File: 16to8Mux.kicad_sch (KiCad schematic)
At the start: 4 parts

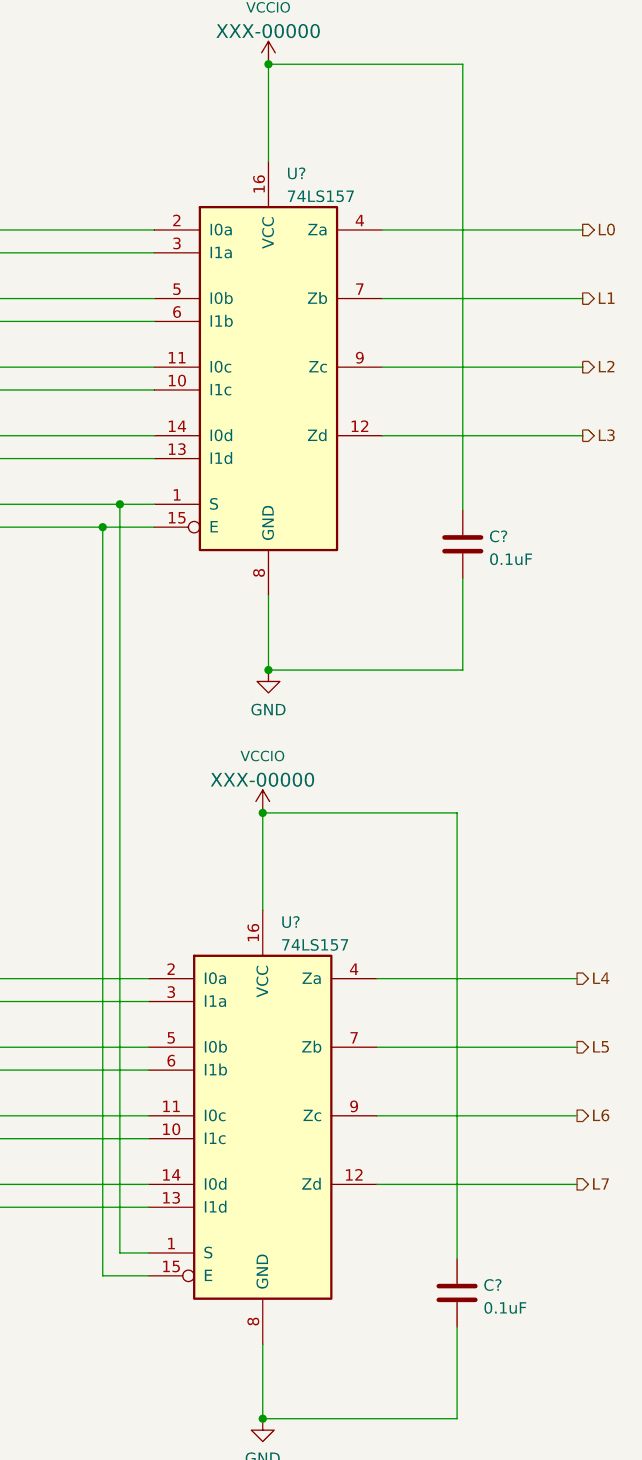
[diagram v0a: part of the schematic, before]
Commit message: Even more simplification and be able to reset feathers separately from the chipset
Makes it possible to also reset them if needed as well
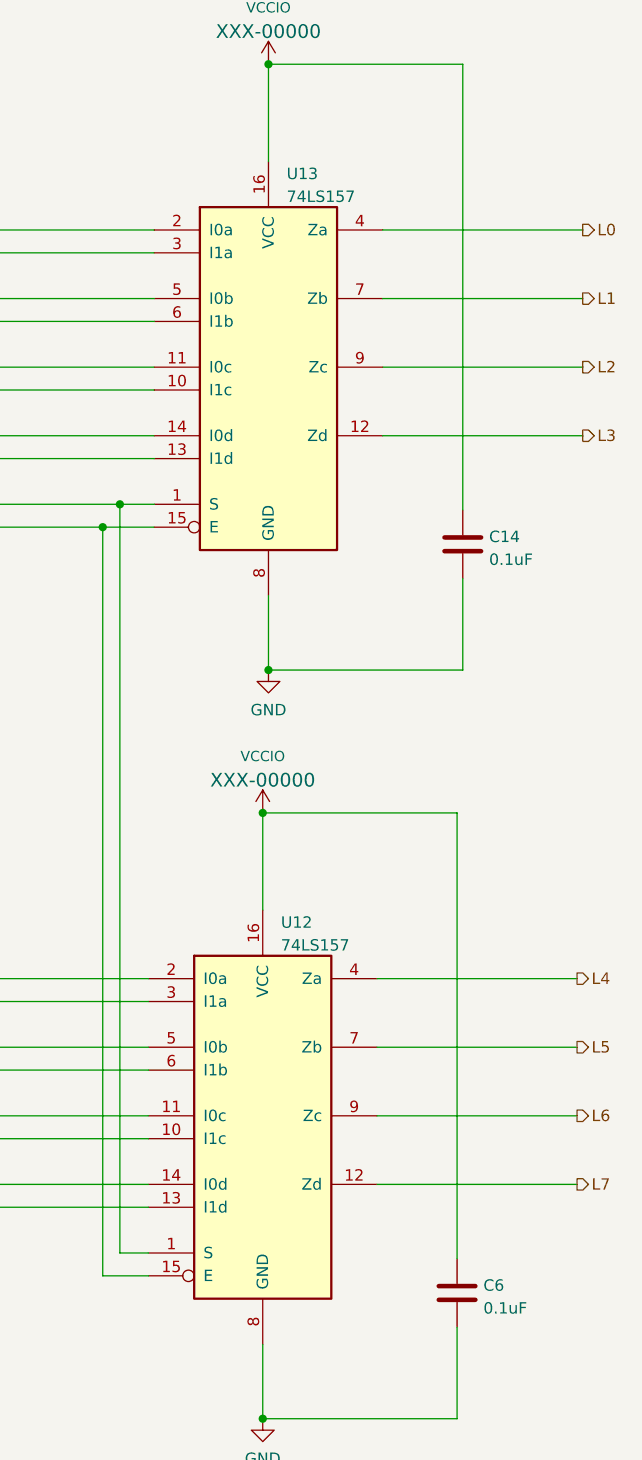
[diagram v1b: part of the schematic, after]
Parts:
- C14, C6: renamed from C?; footprint (none) -> Capacitor_SMD:C_0805_2012Metric_Pad1.18x1.45mm_HandSolder
- U12, U13: renamed from U?; footprint (none) -> Package_DIP:DIP-16_W7.62mm_Socket
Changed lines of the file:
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@@
   (symbol (lib_id "Device:C") (at 99.06 85.09 0) (unit 1)
     (in_bom yes) (on_board yes) (fields_autoplaced)
-    (property "Reference" "C?" (id 0) (at 101.981 84.2553 0)
+    (property "Reference" "C14" (id 0) (at 101.981 84.2553 0)
       (effects (font (size 1.27 1.27)) (justify left))
     )
@@
       (effects (font (size 1.27 1.27)) (justify left))
     )
-    (property "Footprint" "" (id 2) (at 100.0252 88.9 0)
+    (property "Footprint" "Capacitor_SMD:C_0805_2012Metric_Pad1.18x1.45mm_HandSolder" (id 2) (at 100.0252 88.9 0)
       (effects (font (size 1.27 1.27)) hide)
     )
@@
   (symbol (lib_id "power:GND") (at 76.835 182.245 0) (unit 1)
     (in_bom yes) (on_board yes) (fields_autoplaced)
-    (property "Reference" "#PWR?" (id 0) (at 76.835 188.595 0)
+    (property "Reference" "#PWR038" (id 0) (at 76.835 188.595 0)
       (effects (font (size 1.27 1.27)) hide)
     )
@@
   (symbol (lib_id "power:GND") (at 77.47 99.06 0) (unit 1)
     (in_bom yes) (on_board yes) (fields_autoplaced)
-    (property "Reference" "#PWR?" (id 0) (at 77.47 105.41 0)
+    (property "Reference" "#PWR039" (id 0) (at 77.47 105.41 0)
       (effects (font (size 1.27 1.27)) hide)
     )
@@
   (symbol (lib_id "SparkFun-PowerSymbols:VCCIO") (at 77.47 31.75 0) (unit 1)
     (in_bom yes) (on_board yes) (fields_autoplaced)
-    (property "Reference" "#SUPPLY?" (id 0) (at 78.74 31.75 0)
+    (property "Reference" "#SUPPLY07" (id 0) (at 78.74 31.75 0)
       (effects (font (size 1.143 1.143)) (justify left bottom) hide)
     )
@@
   (symbol (lib_id "Device:C") (at 98.425 168.275 0) (unit 1)
     (in_bom yes) (on_board yes) (fields_autoplaced)
-    (property "Reference" "C?" (id 0) (at 101.346 167.4403 0)
+    (property "Reference" "C6" (id 0) (at 101.346 167.4403 0)
       (effects (font (size 1.27 1.27)) (justify left))
     )
@@
       (effects (font (size 1.27 1.27)) (justify left))
     )
-    (property "Footprint" "" (id 2) (at 99.3902 172.085 0)
+    (property "Footprint" "Capacitor_SMD:C_0805_2012Metric_Pad1.18x1.45mm_HandSolder" (id 2) (at 99.3902 172.085 0)
       (effects (font (size 1.27 1.27)) hide)
     )
@@
   (symbol (lib_id "74xx:74LS157") (at 76.835 148.59 0) (unit 1)
     (in_bom yes) (on_board yes) (fields_autoplaced)
-    (property "Reference" "U?" (id 0) (at 78.8544 127.1102 0)
+    (property "Reference" "U12" (id 0) (at 78.8544 127.1102 0)
       (effects (font (size 1.27 1.27)) (justify left))
     )
@@
       (effects (font (size 1.27 1.27)) (justify left))
     )
-    (property "Footprint" "" (id 2) (at 76.835 148.59 0)
+    (property "Footprint" "Package_DIP:DIP-16_W7.62mm_Socket" (id 2) (at 76.835 148.59 0)
       (effects (font (size 1.27 1.27)) hide)
     )
@@
   (symbol (lib_id "SparkFun-PowerSymbols:VCCIO") (at 76.835 114.935 0) (unit 1)
     (in_bom yes) (on_board yes) (fields_autoplaced)
-    (property "Reference" "#SUPPLY?" (id 0) (at 78.105 114.935 0)
+    (property "Reference" "#SUPPLY06" (id 0) (at 78.105 114.935 0)
       (effects (font (size 1.143 1.143)) (justify left bottom) hide)
     )
@@
   (symbol (lib_id "74xx:74LS157") (at 77.47 65.405 0) (unit 1)
     (in_bom yes) (on_board yes) (fields_autoplaced)
-    (property "Reference" "U?" (id 0) (at 79.4894 43.9252 0)
+    (property "Reference" "U13" (id 0) (at 79.4894 43.9252 0)
       (effects (font (size 1.27 1.27)) (justify left))
     )
@@
       (effects (font (size 1.27 1.27)) (justify left))
     )
-    (property "Footprint" "" (id 2) (at 77.47 65.405 0)
+    (property "Footprint" "Package_DIP:DIP-16_W7.62mm_Socket" (id 2) (at 77.47 65.405 0)
       (effects (font (size 1.27 1.27)) hide)
     )

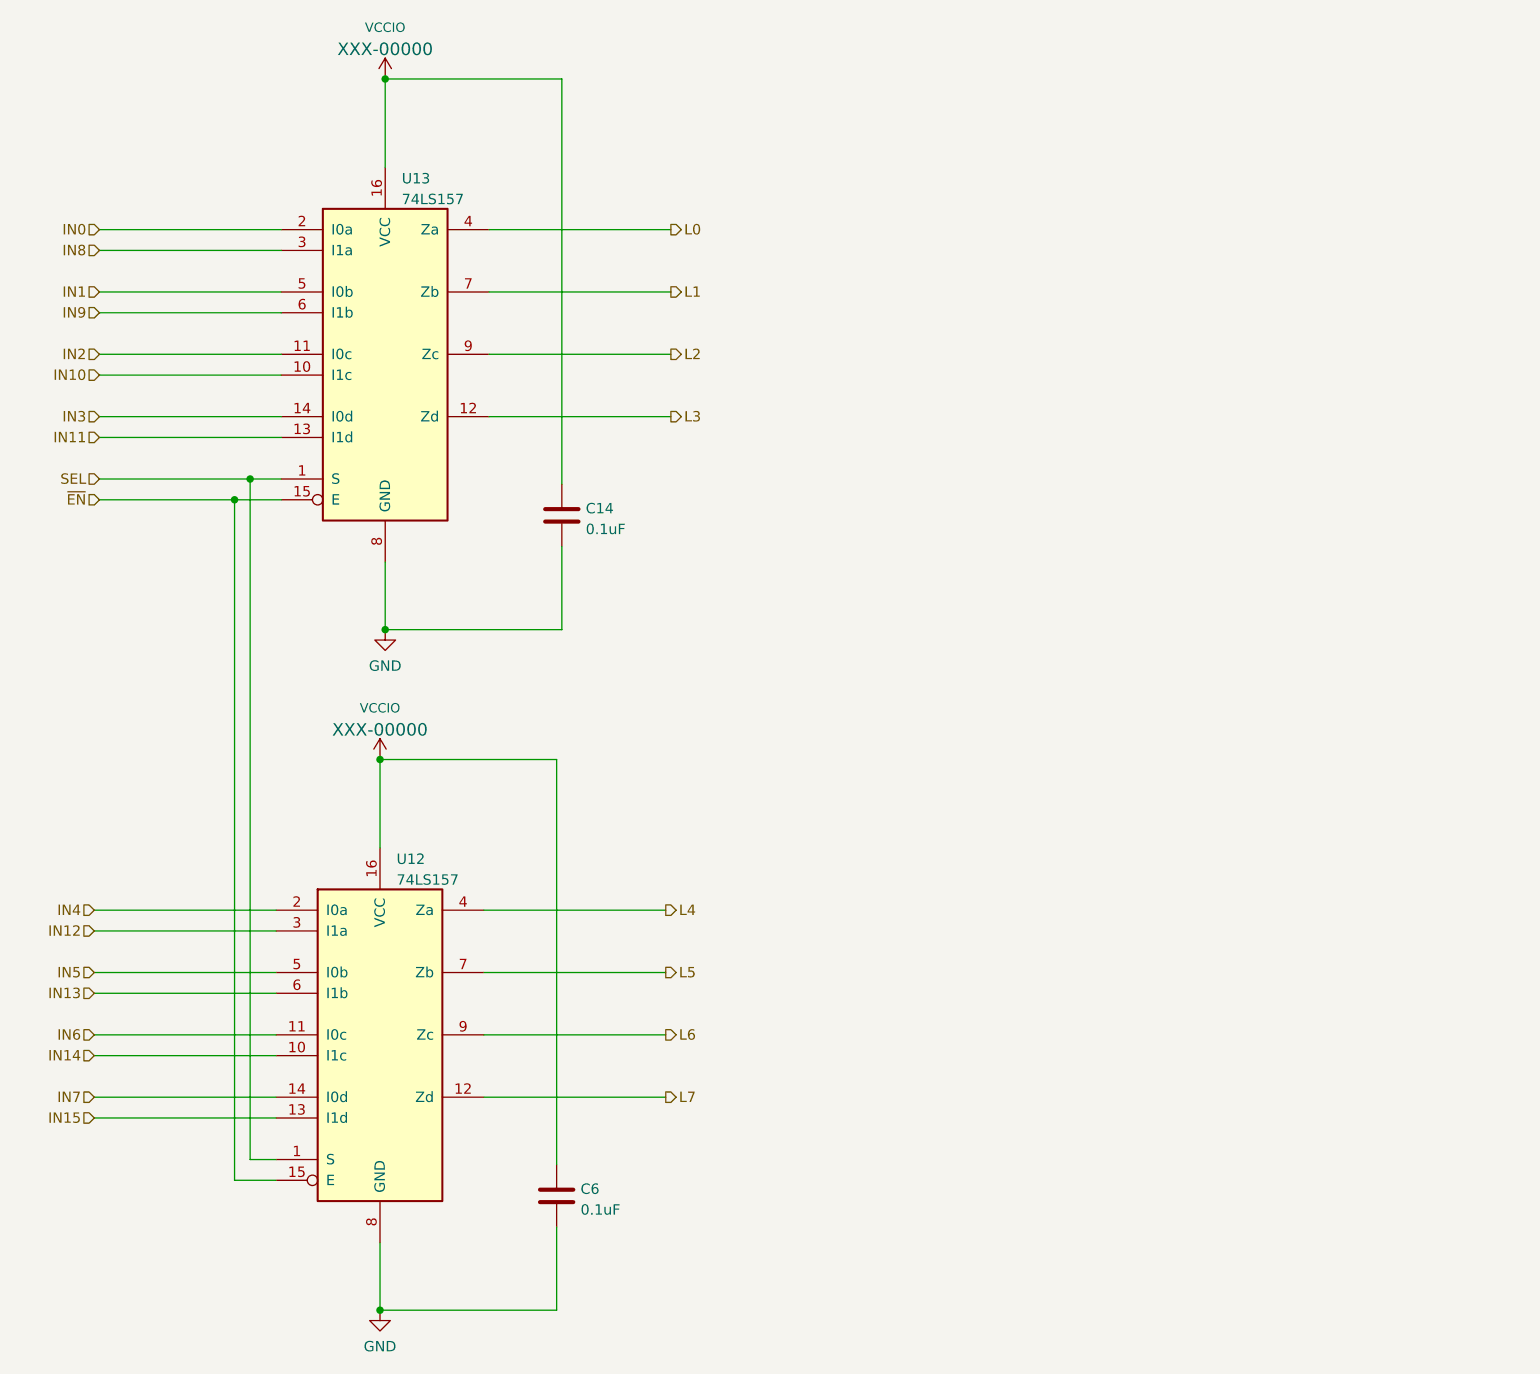
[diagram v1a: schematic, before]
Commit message: Using GALs for address multiplexing seems much simpler and easier to work with
It only requires four gals + an AHC245 to do logic level conversion

Each GAL provides two bits to the 245 where each bit in the 8-bit
quantity is actually four bits apart in reality. It requires a very
simple table lookup followed by a shift by 0, 1, 2, 3 for each 8-bit
quantity respectively.
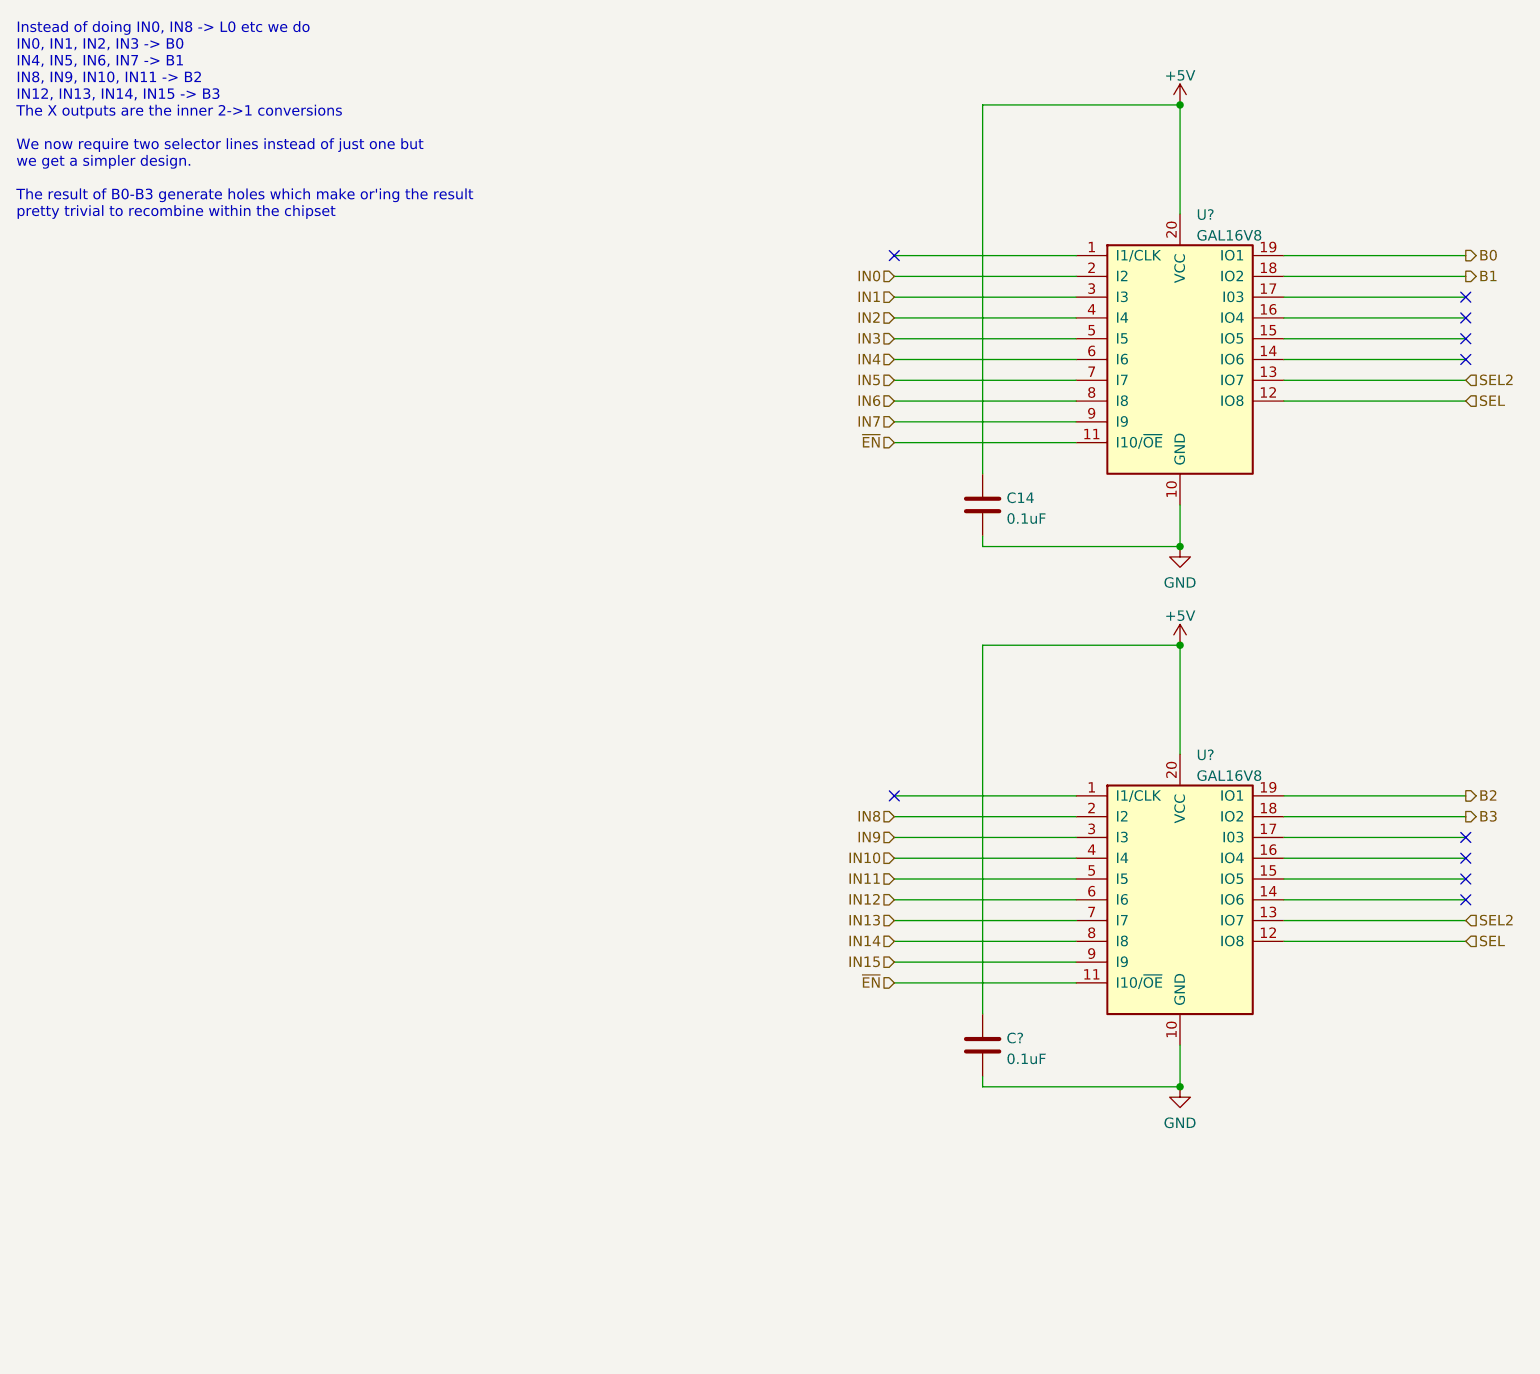
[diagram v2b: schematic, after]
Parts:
- removed C6: 0.1uF, Capacitor_SMD:C_0805_2012Metric_Pad1.18x1.45mm_HandSolder, symbol Device:C
- removed U12, U13: 74LS157, Package_DIP:DIP-16_W7.62mm_Socket, symbol 74xx:74LS157
- added C?: 0.1uF, Capacitor_SMD:C_0805_2012Metric_Pad1.18x1.45mm_HandSolder, symbol Device:C
- added U? (x2): GAL16V8, Package_DIP:DIP-20_W7.62mm_Socket, symbol Logic_Programmable:GAL16V8
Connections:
- net GND: now also C?.2, U?.10 (GND), U?.10 (GND)
- net IN0: now also U?.2 (I2)
- net IN1: now also U?.3 (I3)
- net IN10: now also U?.4 (I4)
- net IN11: now also U?.5 (I5)
- net IN12: now also U?.6 (I6)
- net IN13: now also U?.7 (I7)
- net IN14: now also U?.8 (I8)
- net IN15: now also U?.9 (I9)
- net IN2: now also U?.4 (I4)
- net IN3: now also U?.5 (I5)
- net IN4: now also U?.6 (I6)
- net IN5: now also U?.7 (I7)
- net IN6: now also U?.8 (I8)
- net IN7: now also U?.9 (I9)
- net IN8: now also U?.2 (I2)
- net IN9: now also U?.3 (I3)
- net SEL: now also U?.12 (IO8), U?.12 (IO8)
- net ~{EN}: now also U?.11 (I10/~{OE}), U?.11 (I10/~{OE})
- net VCCIO renamed +5V
- net +5V: now also C?.1, U?.20 (VCC), U?.20 (VCC)
- new net B0: U?.19 (IO1)
- new net B1: U?.18 (IO2)
- new net B2: U?.19 (IO1)
- new net B3: U?.18 (IO2)
- new net SEL2: U?.13 (IO7), U?.13 (IO7)
- no-connect marks 0 -> 10
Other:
- note added: "Instead of doing IN0, IN8 -> L0 etc we do IN0, IN1, IN2, IN3 -> B0 IN4, IN5, IN6, IN7 -> B1 IN8, IN9, IN10, IN11 -> B2 IN12, IN13, IN14, IN15 -> B3 The X outputs are the inner 2->1 conversions We now require two selector lines instead of just one but we get a simpler design. The result of B0-B3 generate holes which make or'ing the result pretty trivial to recombine within the chipset"
- moved on the sheet: C14
